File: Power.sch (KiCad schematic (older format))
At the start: 0 parts

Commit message: Created the first schematic in both Power modules
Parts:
- added C? (x2): C, ~, symbol C
- added F? (x4): FUSE, ~, symbol FUSE
- added L? (x2): INDUCTOR, ~, symbol INDUCTOR
- added P?: CONN_12X2, symbol CONN_12X2
- added R?: R, ~, symbol R
- added SW?: SWITCH_INV, ~, symbol SWITCH_INV
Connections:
- net labels added: +12P, +12V, +3.3V, +5V, -12P, -12V, GND
- wire segments 0 -> 43

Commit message: Modified the FAN module and corresponding pins in Arduino module
1) Added FAN_MODE
2) Changed FAN_EN_N to FAN_PWM
3) Used one of the digital PWM pins for FAN_PWM
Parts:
- removed F? (x4): FUSE, ~, symbol FUSE
- added TH? (x4): THERMISTOR, ~, symbol THERMISTOR
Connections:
- net labels added: +12C
- wire segments 43 -> 50
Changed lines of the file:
@@
 Sheet 4 9
 Title ""
-Date "10 feb 2014"
+Date "11 feb 2014"
 Rev ""
 Comp ""
@@
 L +3.3V #PWR?
 U 1 1 52F76770
-P 4750 1550
-F 0 "#PWR?" H 4750 1510 30  0001 C CNN
-F 1 "+3.3V" H 4750 1660 30  0000 C CNN
-F 2 "" H 4750 1550 60  0000 C CNN
-F 3 "" H 4750 1550 60  0000 C CNN
-	1    4750 1550
+P 5150 1550
+F 0 "#PWR?" H 5150 1510 30  0001 C CNN
+F 1 "+3.3V" H 5150 1660 30  0000 C CNN
+F 2 "" H 5150 1550 60  0000 C CNN
+F 3 "" H 5150 1550 60  0000 C CNN
+	1    5150 1550
 	1    0    0    -1
 $EndComp
@@
 	2800 2150 2800 1950
 $Comp
-L FUSE F?
-U 1 1 52F767BA
-P 4350 1850
-F 0 "F?" H 4450 1900 40  0000 C CNN
-F 1 "FUSE" H 4250 1800 40  0000 C CNN
-F 2 "~" H 4350 1850 60  0000 C CNN
-F 3 "~" H 4350 1850 60  0000 C CNN
-	1    4350 1850
-	1    0    0    -1
-$EndComp
-$Comp
-L FUSE F?
-U 1 1 52F767C9
-P 5050 2050
-F 0 "F?" H 5150 2100 40  0000 C CNN
-F 1 "FUSE" H 4950 2000 40  0000 C CNN
-F 2 "~" H 5050 2050 60  0000 C CNN
-F 3 "~" H 5050 2050 60  0000 C CNN
-	1    5050 2050
-	1    0    0    -1
-$EndComp
-$Comp
 L SWITCH_INV SW?
 U 1 1 52F767D8
@@
 $EndComp
 Wire Wire Line
-	3950 1850 4100 1850
-Wire Wire Line
-	4600 1850 4750 1850
-Wire Wire Line
-	4750 1850 4750 1550
-Wire Wire Line
-	3950 2050 4800 2050
+	3950 1850 4050 1850
+Wire Wire Line
+	4050 1850 4400 1850
+Wire Wire Line
+	4900 1850 5150 1850
+Wire Wire Line
+	5150 1850 5150 1550
+Wire Wire Line
+	3950 2050 4150 2050
+Wire Wire Line
+	4150 2050 4800 2050
 Wire Wire Line
 	3950 1950 4150 1950
@@
 Wire Wire Line
 	5450 2050 5450 1550
-$Comp
-L FUSE F?
-U 1 1 52F76849
-P 5850 2250
-F 0 "F?" H 5950 2300 40  0000 C CNN
-F 1 "FUSE" H 5750 2200 40  0000 C CNN
-F 2 "~" H 5850 2250 60  0000 C CNN
-F 3 "~" H 5850 2250 60  0000 C CNN
-	1    5850 2250
-	1    0    0    -1
-$EndComp
-$Comp
-L FUSE F?
-U 1 1 52F7684F
-P 6750 2450
-F 0 "F?" H 6850 2500 40  0000 C CNN
-F 1 "FUSE" H 6650 2400 40  0000 C CNN
-F 2 "~" H 6750 2450 60  0000 C CNN
-F 3 "~" H 6750 2450 60  0000 C CNN
-	1    6750 2450
-	1    0    0    -1
-$EndComp
-Wire Wire Line
-	5600 2250 3950 2250
+Wire Wire Line
+	5600 2250 4350 2250
+Wire Wire Line
+	4350 2250 3950 2250
 Wire Wire Line
 	6100 2250 6250 2250
@@
 	8100 3000 8600 3000
 Wire Wire Line
-	9200 3000 10150 3000
+	9200 3000 9350 3000
+Wire Wire Line
+	9350 3000 10150 3000
 Wire Wire Line
 	9350 3000 9350 3050
 Wire Wire Line
-	9350 3450 9350 3700
+	9350 3450 9350 3550
+Wire Wire Line
+	9350 3550 9350 3700
 Wire Wire Line
 	9350 3550 8900 3550
@@
 Connection ~ 9350 3550
 Wire Wire Line
-	9200 4200 10200 4200
+	9200 4200 9350 4200
+Wire Wire Line
+	9350 4200 10200 4200
 Wire Wire Line
 	9350 4200 9350 4100
@@
 Wire Wire Line
 	10200 4200 10200 4450
+Wire Wire Line
+	4350 2250 4350 1600
+Connection ~ 4350 2250
+$Comp
+L +12C #PWR?
+U 1 1 52F9D553
+P 4350 1600
+F 0 "#PWR?" H 4350 1570 30  0001 C CNN
+F 1 "+12C" H 4350 1710 40  0000 C CNN
+F 2 "" H 4350 1600 60  0000 C CNN
+F 3 "" H 4350 1600 60  0000 C CNN
+	1    4350 1600
+	1    0    0    -1
+$EndComp
+$Comp
+L THERMISTOR TH?
+U 1 1 52F9DF34
+P 4650 1850
+F 0 "TH?" V 4750 1900 50  0000 C CNN
+F 1 "THERMISTOR" V 4550 1850 50  0000 C CNN
+F 2 "~" H 4650 1850 60  0000 C CNN
+F 3 "~" H 4650 1850 60  0000 C CNN
+	1    4650 1850
+	0    -1   -1   0
+$EndComp
+$Comp
+L THERMISTOR TH?
+U 1 1 52F9DF41
+P 5050 2050
+F 0 "TH?" V 5150 2100 50  0000 C CNN
+F 1 "THERMISTOR" V 4950 2050 50  0000 C CNN
+F 2 "~" H 5050 2050 60  0000 C CNN
+F 3 "~" H 5050 2050 60  0000 C CNN
+	1    5050 2050
+	0    -1   -1   0
+$EndComp
+$Comp
+L THERMISTOR TH?
+U 1 1 52F9DF47
+P 5850 2250
+F 0 "TH?" V 5950 2300 50  0000 C CNN
+F 1 "THERMISTOR" V 5750 2250 50  0000 C CNN
+F 2 "~" H 5850 2250 60  0000 C CNN
+F 3 "~" H 5850 2250 60  0000 C CNN
+	1    5850 2250
+	0    -1   -1   0
+$EndComp
+$Comp
+L THERMISTOR TH?
+U 1 1 52F9DF57
+P 6750 2450
+F 0 "TH?" V 6850 2500 50  0000 C CNN
+F 1 "THERMISTOR" V 6650 2450 50  0000 C CNN
+F 2 "~" H 6750 2450 60  0000 C CNN
+F 3 "~" H 6750 2450 60  0000 C CNN
+	1    6750 2450
+	0    -1   -1   0
+$EndComp
 $EndSCHEMATC

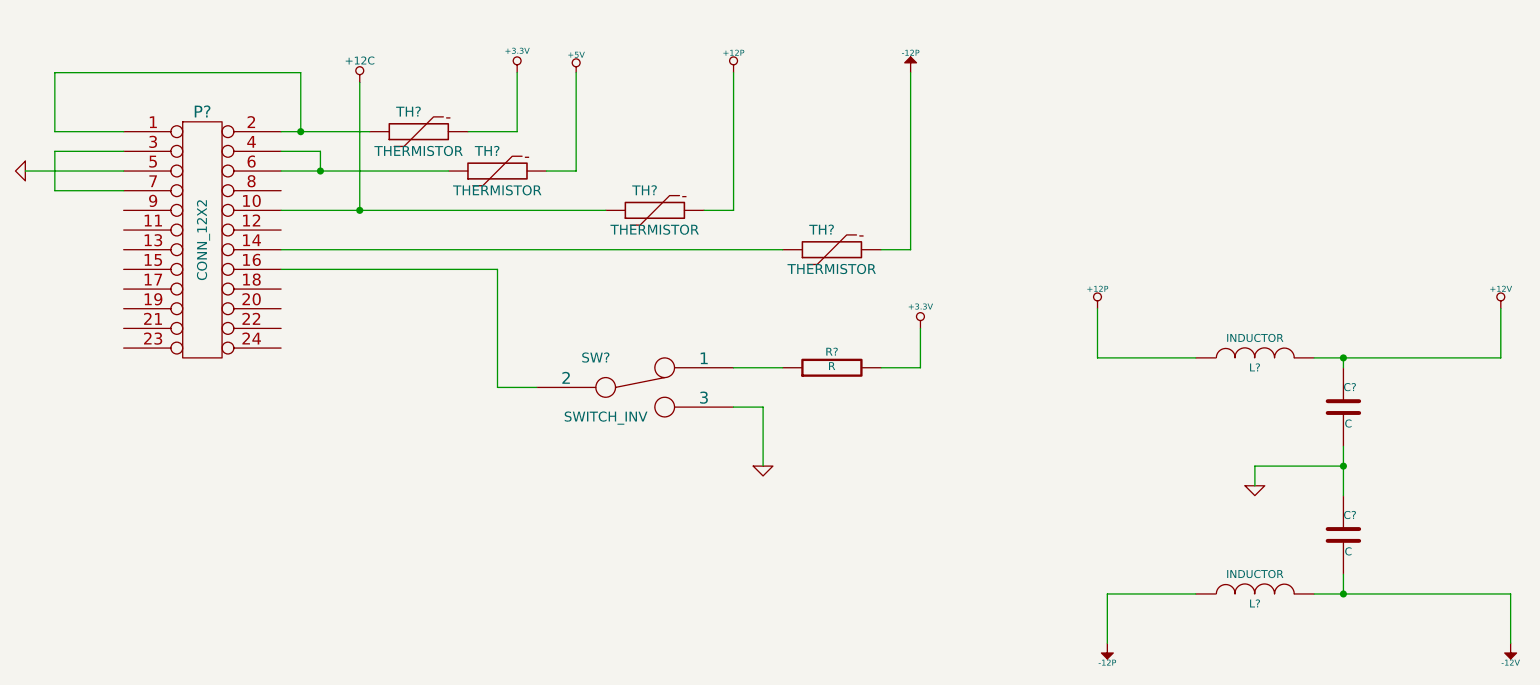
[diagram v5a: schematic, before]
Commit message: RELAY 02-20-2014
1) Created and associated footprints for relay module
2) Placed relay module's components in PCB layout
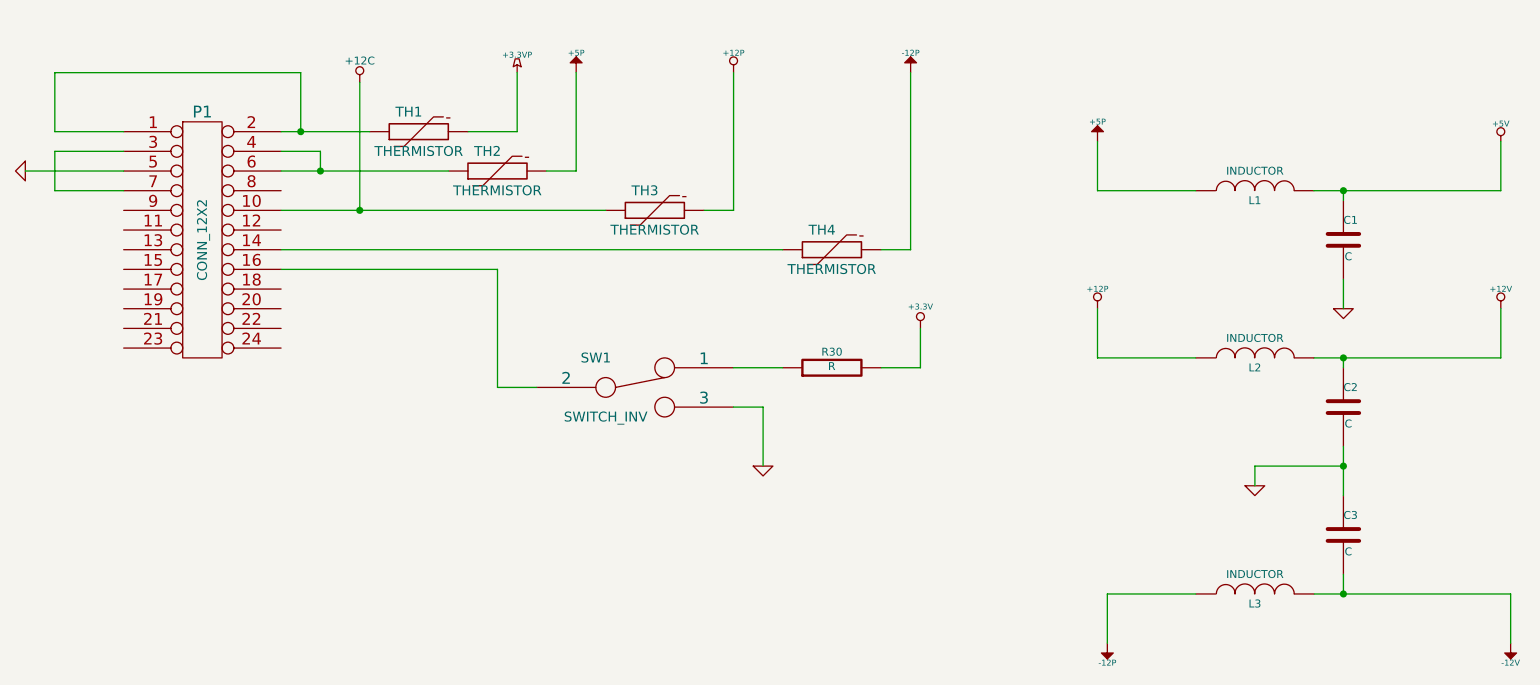
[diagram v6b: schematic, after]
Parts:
- added C1: C, ~, symbol C
- added L1: INDUCTOR, ~, symbol INDUCTOR
- gave numbers to parts that had none: 11
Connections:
- net +3.3V: no longer TH1.2
- net +5V: now also C1.1, L1.2; no longer TH2.2
- net GND: now also C1.2
- new net +3.3VP: TH1.2
- new net +5P: L1.1, TH2.2
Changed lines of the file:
@@
 Sheet 4 9
 Title ""
-Date "11 feb 2014"
+Date "20 feb 2014"
 Rev ""
 Comp ""
@@
 $EndDescr
 $Comp
-L CONN_12X2 P?
+L CONN_12X2 P1
 U 1 1 52F76716
 P 3550 2400
-F 0 "P?" H 3550 3050 60  0000 C CNN
+F 0 "P1" H 3550 3050 60  0000 C CNN
 F 1 "CONN_12X2" V 3550 2400 50  0000 C CNN
 F 2 "" H 3550 2400 60  0000 C CNN
@@
 $EndComp
 $Comp
-L GND #PWR?
+L GND #PWR17
 U 1 1 52F7672F
 P 2650 2050
-F 0 "#PWR?" H 2650 2050 30  0001 C CNN
+F 0 "#PWR17" H 2650 2050 30  0001 C CNN
 F 1 "GND" H 2650 1980 30  0001 C CNN
 F 2 "" H 2650 2050 60  0000 C CNN
@@
 $EndComp
 $Comp
-L +3.3V #PWR?
-U 1 1 52F76770
-P 5150 1550
-F 0 "#PWR?" H 5150 1510 30  0001 C CNN
-F 1 "+3.3V" H 5150 1660 30  0000 C CNN
-F 2 "" H 5150 1550 60  0000 C CNN
-F 3 "" H 5150 1550 60  0000 C CNN
-	1    5150 1550
-	1    0    0    -1
-$EndComp
-$Comp
-L +5V #PWR?
+L +5V #PWR30
 U 1 1 52F7677F
-P 5450 1550
-F 0 "#PWR?" H 5450 1640 20  0001 C CNN
-F 1 "+5V" H 5450 1640 30  0000 C CNN
-F 2 "" H 5450 1550 60  0000 C CNN
-F 3 "" H 5450 1550 60  0000 C CNN
-	1    5450 1550
+P 10150 1900
+F 0 "#PWR30" H 10150 1990 20  0001 C CNN
+F 1 "+5V" H 10150 1990 30  0000 C CNN
+F 2 "" H 10150 1900 60  0000 C CNN
+F 3 "" H 10150 1900 60  0000 C CNN
+	1    10150 1900
 	1    0    0    -1
 $EndComp
@@
 	2800 2150 2800 1950
 $Comp
-L SWITCH_INV SW?
+L SWITCH_INV SW1
 U 1 1 52F767D8
 P 5750 3150
-F 0 "SW?" H 5550 3300 50  0000 C CNN
+F 0 "SW1" H 5550 3300 50  0000 C CNN
 F 1 "SWITCH_INV" H 5600 3000 50  0000 C CNN
 F 2 "~" H 5750 3150 60  0000 C CNN
@@
 $EndComp
 Wire Wire Line
-	3950 1850 4050 1850
-Wire Wire Line
-	4050 1850 4400 1850
+	3950 1850 4400 1850
 Wire Wire Line
 	4900 1850 5150 1850
@@
 	5150 1850 5150 1550
 Wire Wire Line
-	3950 2050 4150 2050
-Wire Wire Line
-	4150 2050 4800 2050
+	3950 2050 4800 2050
 Wire Wire Line
 	3950 1950 4150 1950
@@
 	5450 2050 5450 1550
 Wire Wire Line
-	5600 2250 4350 2250
-Wire Wire Line
-	4350 2250 3950 2250
+	3950 2250 5600 2250
 Wire Wire Line
 	6100 2250 6250 2250
@@
 	7150 2450 7150 1550
 $Comp
-L -12P #PWR?
+L -12P #PWR23
 U 1 1 52F768E3
 P 7150 1550
-F 0 "#PWR?" H 7150 1680 20  0001 C CNN
+F 0 "#PWR23" H 7150 1680 20  0001 C CNN
 F 1 "-12P" H 7150 1650 30  0000 C CNN
 F 2 "" H 7150 1550 60  0000 C CNN
@@
 $EndComp
 $Comp
-L +12P #PWR?
+L +12P #PWR21
 U 1 1 52F768F2
 P 6250 1550
-F 0 "#PWR?" H 6250 1520 30  0001 C CNN
+F 0 "#PWR21" H 6250 1520 30  0001 C CNN
 F 1 "+12P" H 6250 1650 30  0000 C CNN
 F 2 "" H 6250 1550 60  0000 C CNN
@@
 	5050 3150 5250 3150
 $Comp
-L GND #PWR?
+L GND #PWR22
 U 1 1 52F7693B
 P 6400 3550
-F 0 "#PWR?" H 6400 3550 30  0001 C CNN
+F 0 "#PWR22" H 6400 3550 30  0001 C CNN
 F 1 "GND" H 6400 3480 30  0001 C CNN
 F 2 "" H 6400 3550 60  0000 C CNN
@@
 	6400 3250 6250 3250
 $Comp
-L R R?
+L R R30
 U 1 1 52F76966
 P 6750 3050
-F 0 "R?" V 6830 3050 40  0000 C CNN
+F 0 "R30" V 6830 3050 40  0000 C CNN
 F 1 "R" V 6757 3051 40  0000 C CNN
 F 2 "~" V 6680 3050 30  0000 C CNN
@@
 	6500 3050 6250 3050
 $Comp
-L +3.3V #PWR?
+L +3.3V #PWR24
 U 1 1 52F76991
 P 7200 2850
-F 0 "#PWR?" H 7200 2810 30  0001 C CNN
+F 0 "#PWR24" H 7200 2810 30  0001 C CNN
 F 1 "+3.3V" H 7200 2960 30  0000 C CNN
 F 2 "" H 7200 2850 60  0000 C CNN
@@
 	7200 3050 7200 2850
 $Comp
-L INDUCTOR L?
+L INDUCTOR L2
 U 1 1 52F769B8
 P 8900 3000
-F 0 "L?" V 8850 3000 40  0000 C CNN
+F 0 "L2" V 8850 3000 40  0000 C CNN
 F 1 "INDUCTOR" V 9000 3000 40  0000 C CNN
 F 2 "~" H 8900 3000 60  0000 C CNN
@@
 $EndComp
 $Comp
-L C C?
+L C C2
 U 1 1 52F769CC
 P 9350 3250
-F 0 "C?" H 9350 3350 40  0000 L CNN
+F 0 "C2" H 9350 3350 40  0000 L CNN
 F 1 "C" H 9356 3165 40  0000 L CNN
 F 2 "~" H 9388 3100 30  0000 C CNN
@@
 $EndComp
 $Comp
-L INDUCTOR L?
+L INDUCTOR L3
 U 1 1 52F769D9
 P 8900 4200
-F 0 "L?" V 8850 4200 40  0000 C CNN
+F 0 "L3" V 8850 4200 40  0000 C CNN
 F 1 "INDUCTOR" V 9000 4200 40  0000 C CNN
 F 2 "~" H 8900 4200 60  0000 C CNN
@@
 $EndComp
 $Comp
-L C C?
+L C C3
 U 1 1 52F769DF
 P 9350 3900
-F 0 "C?" H 9350 4000 40  0000 L CNN
+F 0 "C3" H 9350 4000 40  0000 L CNN
 F 1 "C" H 9356 3815 40  0000 L CNN
 F 2 "~" H 9388 3750 30  0000 C CNN
@@
 $EndComp
 $Comp
-L +12P #PWR?
+L +12P #PWR26
 U 1 1 52F769E7
 P 8100 2750
-F 0 "#PWR?" H 8100 2720 30  0001 C CNN
+F 0 "#PWR26" H 8100 2720 30  0001 C CNN
 F 1 "+12P" H 8100 2850 30  0000 C CNN
 F 2 "" H 8100 2750 60  0000 C CNN
@@
 $EndComp
 $Comp
-L GND #PWR?
+L GND #PWR28
 U 1 1 52F769F6
 P 8900 3650
-F 0 "#PWR?" H 8900 3650 30  0001 C CNN
+F 0 "#PWR28" H 8900 3650 30  0001 C CNN
 F 1 "GND" H 8900 3580 30  0001 C CNN
 F 2 "" H 8900 3650 60  0000 C CNN
@@
 $EndComp
 $Comp
-L -12P #PWR?
+L -12P #PWR27
 U 1 1 52F76A05
 P 8150 4450
-F 0 "#PWR?" H 8150 4580 20  0001 C CNN
+F 0 "#PWR27" H 8150 4580 20  0001 C CNN
 F 1 "-12P" H 8150 4550 30  0000 C CNN
 F 2 "" H 8150 4450 60  0000 C CNN
@@
 	8100 3000 8600 3000
 Wire Wire Line
-	9200 3000 9350 3000
-Wire Wire Line
-	9350 3000 10150 3000
+	9200 3000 10150 3000
 Wire Wire Line
 	9350 3000 9350 3050
 Wire Wire Line
-	9350 3450 9350 3550
-Wire Wire Line
-	9350 3550 9350 3700
+	9350 3450 9350 3700
 Wire Wire Line
 	9350 3550 8900 3550
@@
 Connection ~ 9350 3550
 Wire Wire Line
-	9200 4200 9350 4200
-Wire Wire Line
-	9350 4200 10200 4200
+	9200 4200 10200 4200
 Wire Wire Line
 	9350 4200 9350 4100
@@
 	8150 4200 8150 4450
 $Comp
-L -12V #PWR?
+L -12V #PWR32
 U 1 1 52F76AF7
 P 10200 4450
-F 0 "#PWR?" H 10200 4580 20  0001 C CNN
+F 0 "#PWR32" H 10200 4580 20  0001 C CNN
 F 1 "-12V" H 10200 4550 30  0000 C CNN
 F 2 "" H 10200 4450 60  0000 C CNN
@@
 $EndComp
 $Comp
-L +12V #PWR?
+L +12V #PWR31
 U 1 1 52F76B06
 P 10150 2750
-F 0 "#PWR?" H 10150 2700 20  0001 C CNN
+F 0 "#PWR31" H 10150 2700 20  0001 C CNN
 F 1 "+12V" H 10150 2850 30  0000 C CNN
 F 2 "" H 10150 2750 60  0000 C CNN
@@
 Connection ~ 4350 2250
 $Comp
-L +12C #PWR?
+L +12C #PWR18
 U 1 1 52F9D553
 P 4350 1600
-F 0 "#PWR?" H 4350 1570 30  0001 C CNN
+F 0 "#PWR18" H 4350 1570 30  0001 C CNN
 F 1 "+12C" H 4350 1710 40  0000 C CNN
 F 2 "" H 4350 1600 60  0000 C CNN
@@
 $EndComp
 $Comp
-L THERMISTOR TH?
+L THERMISTOR TH1
 U 1 1 52F9DF34
 P 4650 1850
-F 0 "TH?" V 4750 1900 50  0000 C CNN
+F 0 "TH1" V 4750 1900 50  0000 C CNN
 F 1 "THERMISTOR" V 4550 1850 50  0000 C CNN
 F 2 "~" H 4650 1850 60  0000 C CNN
@@
 $EndComp
 $Comp
-L THERMISTOR TH?
+L THERMISTOR TH2
 U 1 1 52F9DF41
 P 5050 2050
-F 0 "TH?" V 5150 2100 50  0000 C CNN
+F 0 "TH2" V 5150 2100 50  0000 C CNN
 F 1 "THERMISTOR" V 4950 2050 50  0000 C CNN
 F 2 "~" H 5050 2050 60  0000 C CNN
@@
 $EndComp
 $Comp
-L THERMISTOR TH?
+L THERMISTOR TH3
 U 1 1 52F9DF47
 P 5850 2250
-F 0 "TH?" V 5950 2300 50  0000 C CNN
+F 0 "TH3" V 5950 2300 50  0000 C CNN
 F 1 "THERMISTOR" V 5750 2250 50  0000 C CNN
 F 2 "~" H 5850 2250 60  0000 C CNN
@@
 $EndComp
 $Comp
-L THERMISTOR TH?
+L THERMISTOR TH4
 U 1 1 52F9DF57
 P 6750 2450
-F 0 "TH?" V 6850 2500 50  0000 C CNN
+F 0 "TH4" V 6850 2500 50  0000 C CNN
 F 1 "THERMISTOR" V 6650 2450 50  0000 C CNN
 F 2 "~" H 6750 2450 60  0000 C CNN
@@
 	0    -1   -1   0
 $EndComp
+$Comp
+L INDUCTOR L1
+U 1 1 5302E708
+P 8900 2150
+F 0 "L1" V 8850 2150 40  0000 C CNN
+F 1 "INDUCTOR" V 9000 2150 40  0000 C CNN
+F 2 "~" H 8900 2150 60  0000 C CNN
+F 3 "~" H 8900 2150 60  0000 C CNN
+	1    8900 2150
+	0    -1   -1   0
+$EndComp
+$Comp
+L C C1
+U 1 1 5302E70E
+P 9350 2400
+F 0 "C1" H 9350 2500 40  0000 L CNN
+F 1 "C" H 9356 2315 40  0000 L CNN
+F 2 "~" H 9388 2250 30  0000 C CNN
+F 3 "~" H 9350 2400 60  0000 C CNN
+	1    9350 2400
+	1    0    0    -1
+$EndComp
+Wire Wire Line
+	8100 1900 8100 2150
+Wire Wire Line
+	8100 2150 8600 2150
+Wire Wire Line
+	9200 2150 10150 2150
+Wire Wire Line
+	9350 2150 9350 2200
+Wire Wire Line
+	10150 2150 10150 1900
+Connection ~ 9350 2150
+$Comp
+L GND #PWR29
+U 1 1 5302E727
+P 9350 2750
+F 0 "#PWR29" H 9350 2750 30  0001 C CNN
+F 1 "GND" H 9350 2680 30  0001 C CNN
+F 2 "" H 9350 2750 60  0000 C CNN
+F 3 "" H 9350 2750 60  0000 C CNN
+	1    9350 2750
+	1    0    0    -1
+$EndComp
+Wire Wire Line
+	9350 2600 9350 2750
+$Comp
+L +5P #PWR25
+U 1 1 5302E779
+P 8100 1900
+F 0 "#PWR25" H 8100 2030 20  0001 C CNN
+F 1 "+5P" H 8100 2000 30  0000 C CNN
+F 2 "" H 8100 1900 60  0000 C CNN
+F 3 "" H 8100 1900 60  0000 C CNN
+	1    8100 1900
+	1    0    0    -1
+$EndComp
+$Comp
+L +5P #PWR20
+U 1 1 5302E788
+P 5450 1550
+F 0 "#PWR20" H 5450 1680 20  0001 C CNN
+F 1 "+5P" H 5450 1650 30  0000 C CNN
+F 2 "" H 5450 1550 60  0000 C CNN
+F 3 "" H 5450 1550 60  0000 C CNN
+	1    5450 1550
+	1    0    0    -1
+$EndComp
+$Comp
+L +3.3VP #PWR19
+U 1 1 5302E797
+P 5150 1550
+F 0 "#PWR19" H 5200 1580 20  0001 C CNN
+F 1 "+3.3VP" H 5150 1640 30  0000 C CNN
+F 2 "" H 5150 1550 60  0000 C CNN
+F 3 "" H 5150 1550 60  0000 C CNN
+	1    5150 1550
+	1    0    0    -1
+$EndComp
 $EndSCHEMATC

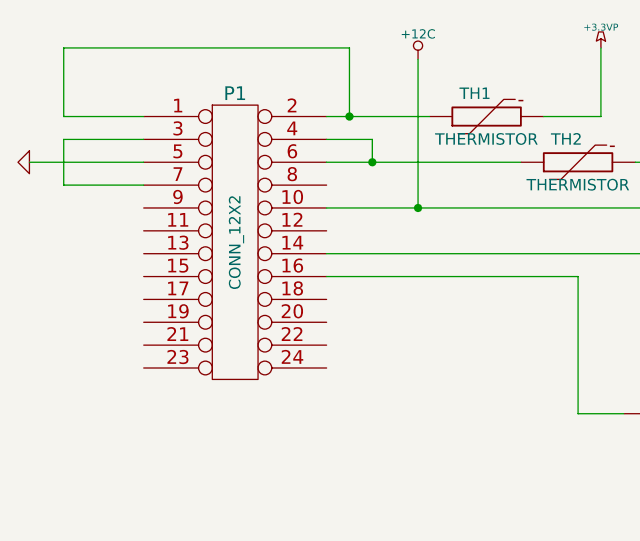
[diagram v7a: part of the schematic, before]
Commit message: Terminal Blocks and ATX Connector
Created footprints for 12pin, 3pin terminal blocks and 24pin ATX Header.
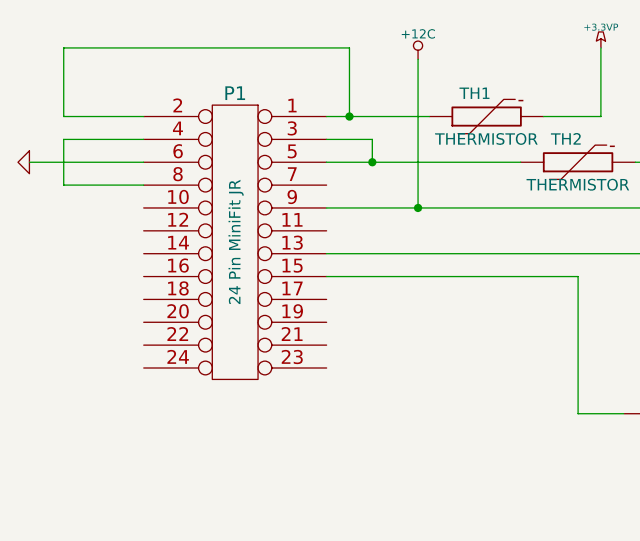
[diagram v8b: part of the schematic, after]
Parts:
- P1: value CONN_12X2 -> 24 Pin MiniFit JR; MFG NAME (none) -> MOLEX; MFG PART NUM (none) -> 39-30-1240
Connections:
- net +12C: now also P1.9 (P9); no longer P1.10 (P10)
- net GND: now also P1.6 (P6); no longer P1.5 (P5)
- net at P1.13 (P13): now also TH4.1
- net at P1.14 (P14): no longer TH4.1
- net at P1.15 (P15): now also SW1.2
- net at P1.16 (P16): no longer SW1.2
- net at P1.3 (P3): now also P1.5 (P5), TH2.1; no longer P1.7 (P7)
- net at P1.8 (P8): now also P1.4 (P4)
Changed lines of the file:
@@
 P 3550 2400
 F 0 "P1" H 3550 3050 60  0000 C CNN
-F 1 "CONN_12X2" V 3550 2400 50  0000 C CNN
+F 1 "24 Pin MiniFit JR" V 3550 2400 50  0000 C CNN
 F 2 "" H 3550 2400 60  0000 C CNN
 F 3 "" H 3550 2400 60  0000 C CNN
+F 4 "MOLEX" H 3550 2400 60  0001 C CNN "MFG NAME"
+F 5 "39-30-1240" H 3550 2400 60  0001 C CNN "MFG PART NUM"
 	1    3550 2400
-	1    0    0    -1
+	-1   0    0    -1
 $EndComp
 $Comp
